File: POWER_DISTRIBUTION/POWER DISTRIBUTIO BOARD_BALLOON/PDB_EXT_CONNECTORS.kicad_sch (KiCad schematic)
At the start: 91 parts, among them J1 Conn_01x02_Socket, J10 Conn_01x02, J11 Conn_01x02, J12 43650-0211, J13 43650-0211, J14 43650-0211, J15 43650-0211, J16 43650-0211, J17 43650-0312, J18 43650-0312, J19 43650-0312, J2 Conn_01x02_Socket, J20 43650-0312, J21 43650-0211, J22 43650-0211, J23 43650-0211, J24 BM12B-GHS-TBT_LF__SN_, J25 43650-0211, J26 BM12B-GHS-TBT_LF__SN_, J27 43650-0211, J28 Conn_01x06, J3 XT90PW-F, J30 Conn_01x02, J31 Conn_01x02, J32 Conn_01x04, J33 Conn_01x02, J34 Conn_01x02, J4 XT90PW-F, J5 Conn_01x02_Socket, J6 XT90PW-F, J7 XT90PW-F, J8 Conn_01x02, J9 Conn_01x02, U4 178.6165.0002, U5 178.6165.0002, U7 USBLC6-2SC6

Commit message: POWER BOARD LAYOUT COMPLETE
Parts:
- removed D7, D9: BAS21, Package_TO_SOT_SMD:SOT-23, symbol Diode:BAS21
- removed R48, R50: 4.7k, Resistor_SMD:R_0603_1608Metric, symbol Device:R_Small

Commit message: added some global labels
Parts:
- added J35, J36: Conn_01x03, Connector_JST:JST_PH_B3B-PH-K_1x03_P2.00mm_Vertical, symbol Connector_Generic:Conn_01x03
- added TP30, TP31: S2761-46R, TestPoint:TestPoint_Pad_2.0x2.0mm, symbol samac_sys:S2761-46R
- J31, J33, J34: footprint Connector_JST:JST_PH_B2B-PH-K_1x02_P2.00mm_Vertical -> Connector_JST:JST_PH_S2B-PH-K_1x02_P2.00mm_Horizontal
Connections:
- net +3V3: now also J35.1 (Pin_1), J36.1 (Pin_1), TP30.1, TP31.1
- net GND: now also J35.3 (Pin_3), J36.3 (Pin_3)
- net PGM_RX: now also J32.2 (Pin_2), U7.6 (I/O1)
- net PGM_TX: now also J32.3 (Pin_3), U7.4 (I/O2)
- new net onewire1: J35.2 (Pin_2)
- new net onewire2: J36.2 (Pin_2)
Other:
- note added: "Silkscreen: ONEWIRE1"
- note added: "Silkscreen:ONEWIRE 2"

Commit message: almost finished wiring
btw for the i2c bus idk if it was meant to be SCL instead of SDL , there is alr an SDA line but i assume so
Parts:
- removed TP25, TP26, TP31: S2761-46R, TestPoint:TestPoint_Pad_2.0x2.0mm, symbol samac_sys:S2761-46R
- J31: footprint Connector_JST:JST_PH_S2B-PH-K_1x02_P2.00mm_Horizontal -> Connector_JST:JST_PH_B2B-PH-K_1x02_P2.00mm_Vertical
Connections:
- net GND: now also D8.1 (A); no longer D10.3 (K), D12.3 (K), D13.3 (K), D8.3 (K), J30.2 (Pin_2), J31.2 (Pin_2), J9.2 (Pin_2), R51.1, R60.1, R61.1
- net PYR_1: no longer J34.1 (Pin_1)
- net PYR_2: now also J34.1 (Pin_1)
- net VBAT+: no longer J33.2 (Pin_2), J34.2 (Pin_2)
- net BAS_IN: now reaches J11.2 (Pin_2), R49.1, TP11.1
- net BAS_IN: now also D8.3 (K); no longer D8.1 (A)
- new net: D10.3 (K), J9.2 (Pin_2), R51.1
- new net: D12.3 (K), J30.2 (Pin_2), R60.1
- new net: D13.3 (K), J31.2 (Pin_2), R61.1
- new net VBAT_Fused_OUT: J33.2 (Pin_2), J34.2 (Pin_2)
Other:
- moved on the sheet: D10, D12, D13, D8

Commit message: edited pcb
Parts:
- removed R49, R51, R60, R61: 4.7k, Resistor_SMD:R_0603_1608Metric, symbol Device:R_Small
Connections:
- net +5V0: now also D10.3 (K), D12.3 (K), D13.3 (K)
- net BAS_IN: no longer D8.3 (K), J11.2 (Pin_2), TP11.1
- net GND: now also J11.2 (Pin_2), J30.2 (Pin_2), J31.2 (Pin_2), J9.2 (Pin_2), TP11.1
- net VBAT+: now also D8.2 (NC), D8.3 (K)
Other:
- moved on the sheet: D10, D12, D8

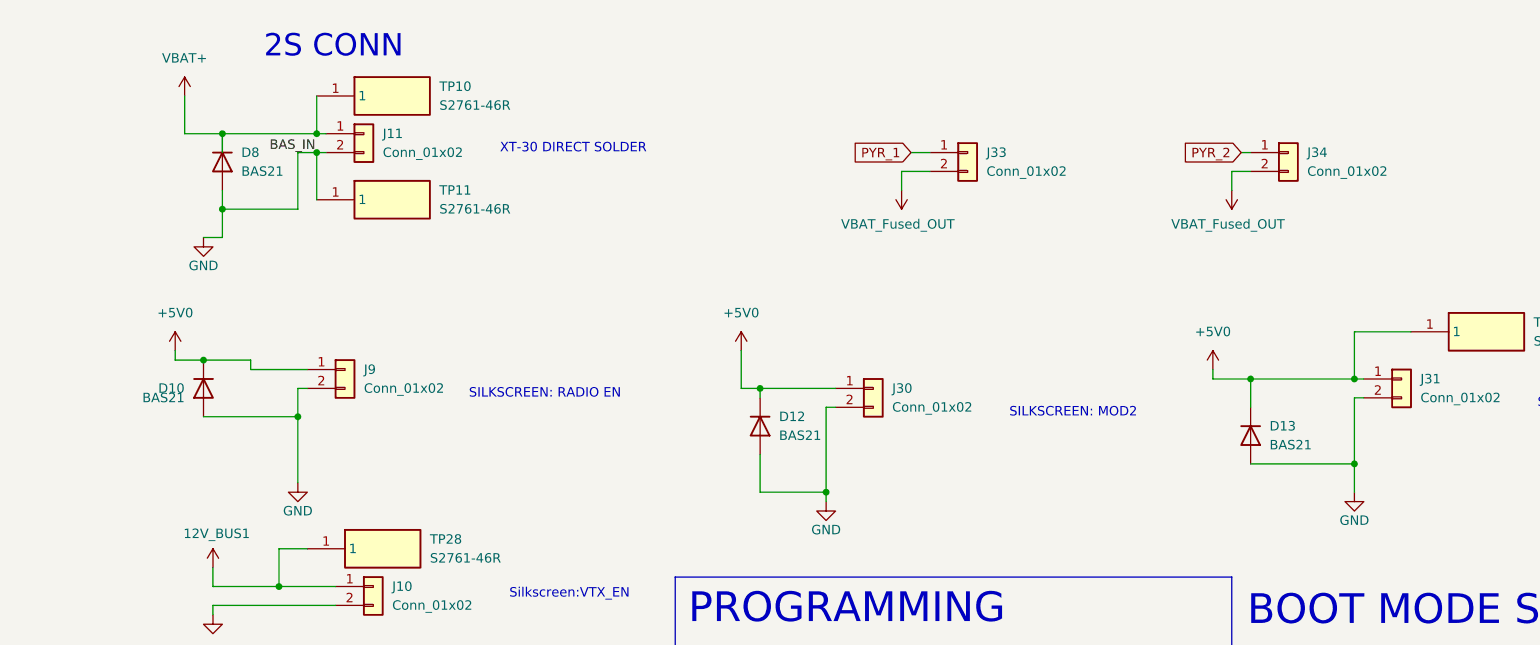
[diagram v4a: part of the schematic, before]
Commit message: edited the BAT to SSC diode
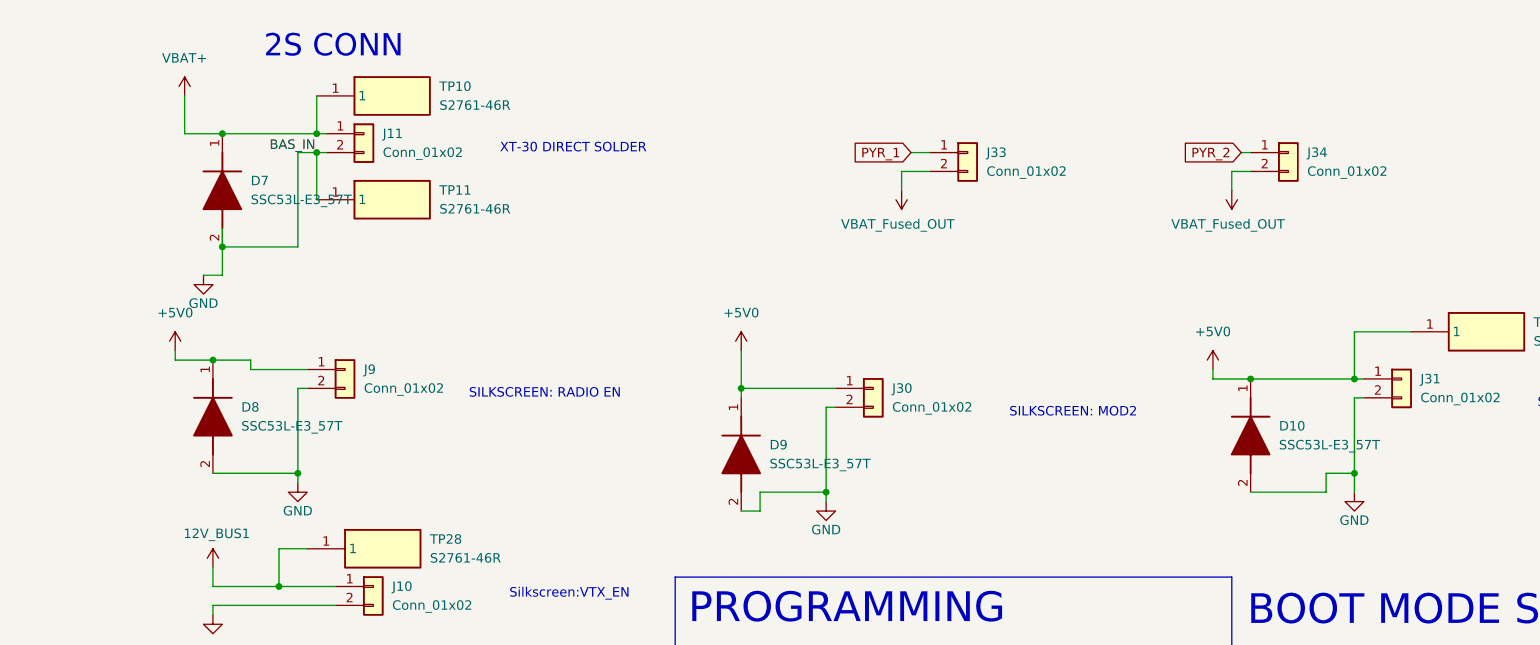
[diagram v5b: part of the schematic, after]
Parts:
- removed D10, D12, D13, D8: BAS21, Package_TO_SOT_SMD:SOT-23, symbol Diode:BAS21
- added D10, D7, D8, D9: SSC53L-E3_57T, DIOM7959X262N, symbol SamacSys_COMMS:SSC53L-E3_57T
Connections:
- net +5V0: now also D10.1 (K), D8.1 (K), D9.1 (K)
- net GND: now also D10.2 (A), D7.2 (A), D8.2 (A), D9.2 (A)
- net VBAT+: now also D7.1 (K)
